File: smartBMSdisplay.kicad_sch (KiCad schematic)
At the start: 7 parts, among them J1 Conn_01x04_Male, J2 Conn_01x05_Male, Q1 BC547, U1 esp32_WROOM

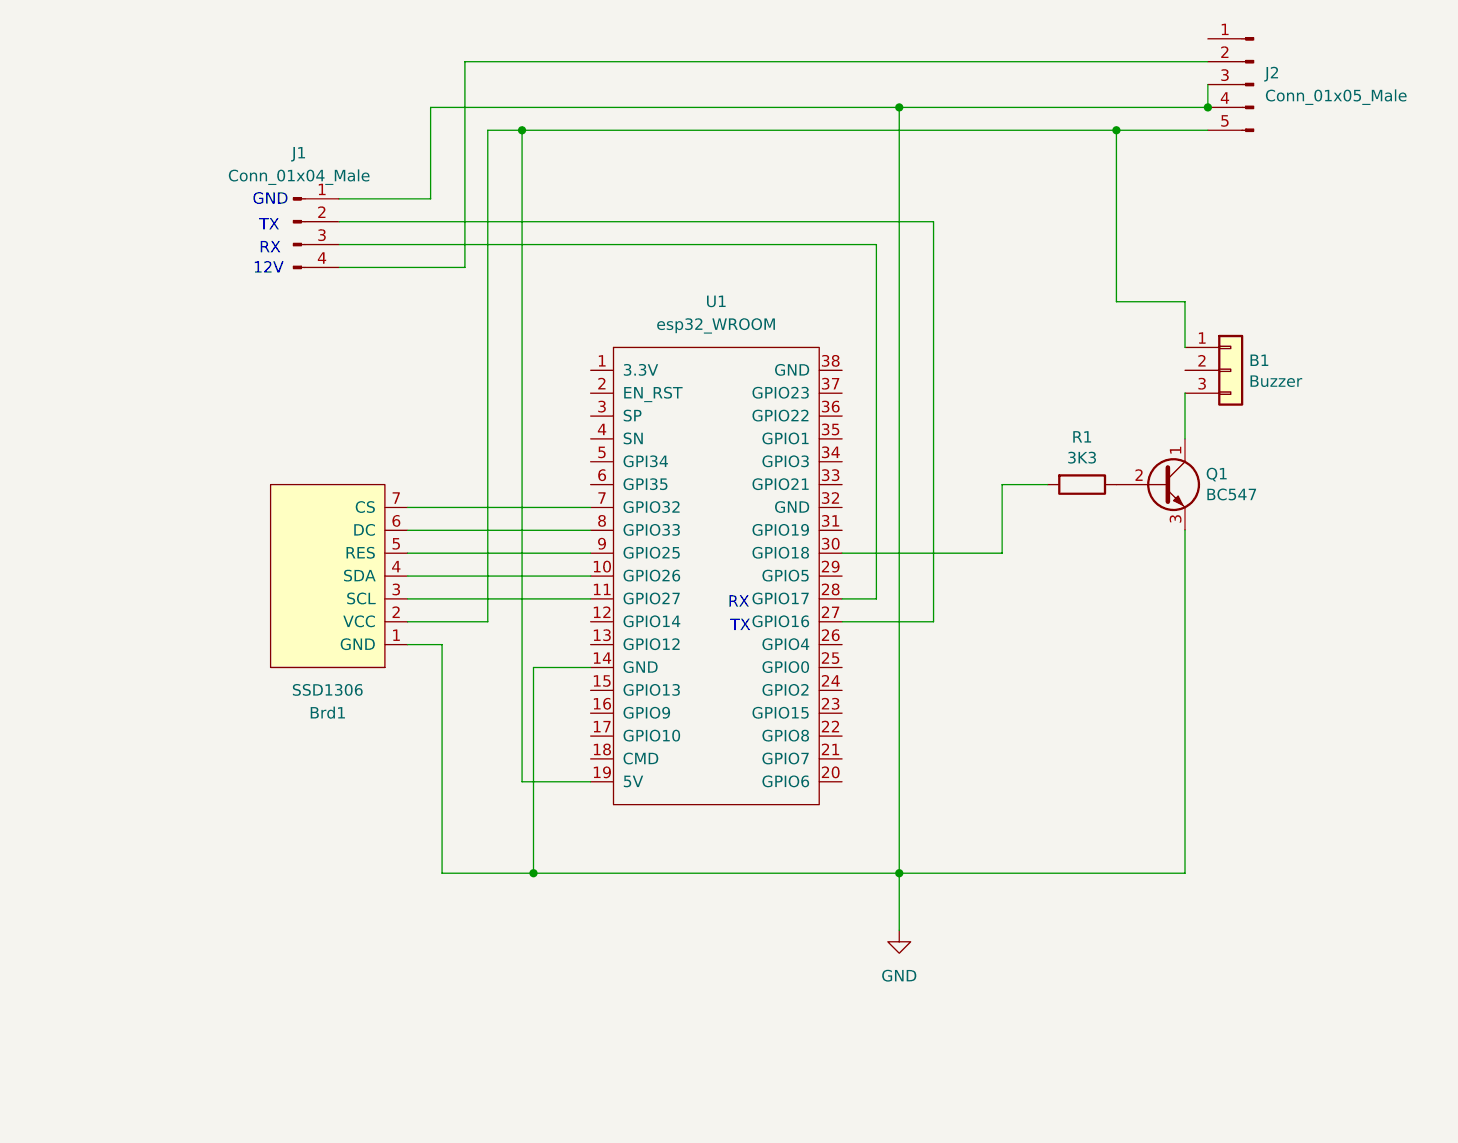
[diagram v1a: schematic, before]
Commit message: Update Readme, misc display changes, update PCB
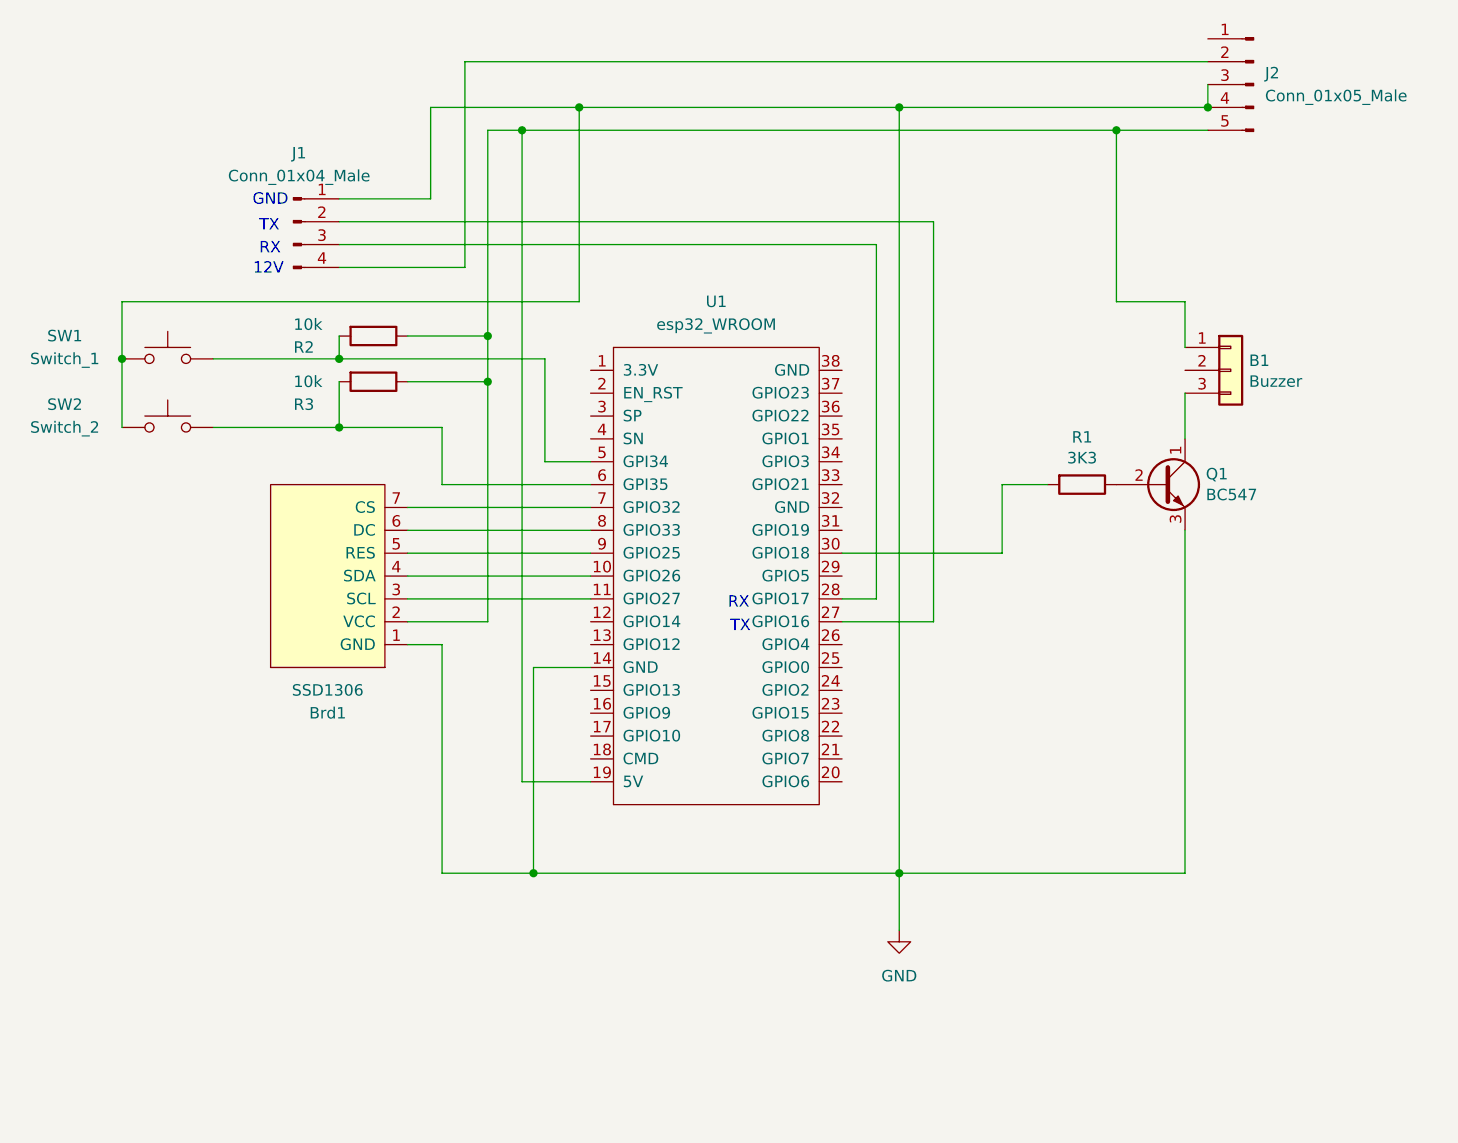
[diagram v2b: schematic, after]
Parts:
- added R2, R3: 10k, Resistor_THT:R_Axial_DIN0207_L6.3mm_D2.5mm_P10.16mm_Horizontal, symbol Device:R
- added SW1: Switch_1, Button_Switch_THT:SW_Tactile_Straight_KSA0Axx1LFTR, symbol Switch:SW_Push
- added SW2: Switch_2, Button_Switch_THT:SW_Tactile_Straight_KSA0Axx1LFTR, symbol Switch:SW_Push
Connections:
- net GND: now also SW1.2, SW2.2
- net at B1.1 (Pin_1), Brd1.2 (VCC), J2.5 (Pin_5)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: now also R2.1, R3.1
- net at U1.5 (GPI34): now also R2.2, SW1.1
- net at U1.6 (GPI35): now also R3.2, SW2.1
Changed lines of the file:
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@@
   (junction (at 144.78 58.42) (diameter 0) (color 0 0 0 0)
   )
+  (junction (at 109.22 58.42) (diameter 0) (color 0 0 0 0)
+  )
   (junction (at 144.78 143.51) (diameter 0) (color 0 0 0 0)
   )
+  (junction (at 82.55 86.36) (diameter 0) (color 0 0 0 0)
+  )
+  (junction (at 58.42 86.36) (diameter 0) (color 0 0 0 0)
+  )
+  (junction (at 82.55 93.98) (diameter 0) (color 0 0 0 0)
+  )
   (junction (at 102.87 60.96) (diameter 0) (color 0 0 0 0)
   )
+  (junction (at 99.06 88.9) (diameter 0) (color 0 0 0 0)
+  )
   (junction (at 168.91 60.96) (diameter 0) (color 0 0 0 0)
   )
+  (junction (at 99.06 83.82) (diameter 0) (color 0 0 0 0)
+  )
+  (wire (pts (xy 109.22 58.42) (xy 144.78 58.42))
+    (stroke (width 0) (type default) (color 0 0 0 0))
+  )
   (wire (pts (xy 176.53 143.51) (xy 144.78 143.51))
     (stroke (width 0) (type default) (color 0 0 0 0))
@@
     (stroke (width 0) (type default) (color 0 0 0 0))
   )
+  (wire (pts (xy 93.98 93.98) (xy 93.98 100.33))
+    (stroke (width 0) (type default) (color 0 0 0 0))
+  )
   (wire (pts (xy 144.78 58.42) (xy 144.78 143.51))
     (stroke (width 0) (type default) (color 0 0 0 0))
   )
+  (wire (pts (xy 68.58 86.36) (xy 82.55 86.36))
+    (stroke (width 0) (type default) (color 0 0 0 0))
+  )
+  (wire (pts (xy 93.98 100.33) (xy 110.49 100.33))
+    (stroke (width 0) (type default) (color 0 0 0 0))
+  )
   (wire (pts (xy 90.17 118.11) (xy 93.98 118.11))
     (stroke (width 0) (type default) (color 0 0 0 0))
@@
     (stroke (width 0) (type default) (color 0 0 0 0))
   )
+  (wire (pts (xy 82.55 83.82) (xy 82.55 86.36))
+    (stroke (width 0) (type default) (color 0 0 0 0))
+  )
   (wire (pts (xy 104.14 120.65) (xy 110.49 120.65))
     (stroke (width 0) (type default) (color 0 0 0 0))
   )
+  (wire (pts (xy 102.87 60.96) (xy 168.91 60.96))
+    (stroke (width 0) (type default) (color 0 0 0 0))
+  )
   (wire (pts (xy 90.17 107.95) (xy 110.49 107.95))
     (stroke (width 0) (type default) (color 0 0 0 0))
   )
-  (wire (pts (xy 102.87 60.96) (xy 168.91 60.96))
-    (stroke (width 0) (type default) (color 0 0 0 0))
-  )
   (wire (pts (xy 168.91 60.96) (xy 168.91 80.01))
     (stroke (width 0) (type default) (color 0 0 0 0))
@@
     (stroke (width 0) (type default) (color 0 0 0 0))
   )
+  (wire (pts (xy 58.42 86.36) (xy 58.42 93.98))
+    (stroke (width 0) (type default) (color 0 0 0 0))
+  )
   (wire (pts (xy 102.87 133.35) (xy 102.87 60.96))
     (stroke (width 0) (type default) (color 0 0 0 0))
   )
+  (wire (pts (xy 90.17 88.9) (xy 99.06 88.9))
+    (stroke (width 0) (type default) (color 0 0 0 0))
+  )
   (wire (pts (xy 90.17 110.49) (xy 110.49 110.49))
     (stroke (width 0) (type default) (color 0 0 0 0))
   )
+  (wire (pts (xy 82.55 93.98) (xy 93.98 93.98))
+    (stroke (width 0) (type default) (color 0 0 0 0))
+  )
   (wire (pts (xy 104.14 143.51) (xy 104.14 120.65))
     (stroke (width 0) (type default) (color 0 0 0 0))
@@
     (stroke (width 0) (type default) (color 0 0 0 0))
   )
+  (wire (pts (xy 96.52 53.34) (xy 179.07 53.34))
+    (stroke (width 0) (type default) (color 0 0 0 0))
+  )
+  (wire (pts (xy 105.41 97.79) (xy 110.49 97.79))
+    (stroke (width 0) (type default) (color 0 0 0 0))
+  )
+  (wire (pts (xy 105.41 86.36) (xy 105.41 97.79))
+    (stroke (width 0) (type default) (color 0 0 0 0))
+  )
   (wire (pts (xy 82.55 71.12) (xy 148.59 71.12))
     (stroke (width 0) (type default) (color 0 0 0 0))
   )
-  (wire (pts (xy 179.07 53.34) (xy 96.52 53.34))
+  (wire (pts (xy 58.42 80.01) (xy 109.22 80.01))
+    (stroke (width 0) (type default) (color 0 0 0 0))
+  )
+  (wire (pts (xy 99.06 83.82) (xy 99.06 60.96))
     (stroke (width 0) (type default) (color 0 0 0 0))
   )
@@
     (stroke (width 0) (type default) (color 0 0 0 0))
   )
+  (wire (pts (xy 68.58 93.98) (xy 82.55 93.98))
+    (stroke (width 0) (type default) (color 0 0 0 0))
+  )
+  (wire (pts (xy 99.06 88.9) (xy 99.06 83.82))
+    (stroke (width 0) (type default) (color 0 0 0 0))
+  )
   (wire (pts (xy 90.17 102.87) (xy 110.49 102.87))
     (stroke (width 0) (type default) (color 0 0 0 0))
   )
+  (wire (pts (xy 82.55 88.9) (xy 82.55 93.98))
+    (stroke (width 0) (type default) (color 0 0 0 0))
+  )
+  (wire (pts (xy 92.71 58.42) (xy 109.22 58.42))
+    (stroke (width 0) (type default) (color 0 0 0 0))
+  )
   (wire (pts (xy 161.29 100.33) (xy 156.21 100.33))
     (stroke (width 0) (type default) (color 0 0 0 0))
@@
     (stroke (width 0) (type default) (color 0 0 0 0))
   )
-  (wire (pts (xy 92.71 58.42) (xy 144.78 58.42))
+  (wire (pts (xy 90.17 83.82) (xy 99.06 83.82))
     (stroke (width 0) (type default) (color 0 0 0 0))
   )
@@
     (stroke (width 0) (type default) (color 0 0 0 0))
   )
+  (wire (pts (xy 82.55 86.36) (xy 105.41 86.36))
+    (stroke (width 0) (type default) (color 0 0 0 0))
+  )
   (wire (pts (xy 156.21 107.95) (xy 138.43 107.95))
     (stroke (width 0) (type default) (color 0 0 0 0))
@@
     (stroke (width 0) (type default) (color 0 0 0 0))
   )
-  (wire (pts (xy 99.06 115.57) (xy 99.06 60.96))
+  (wire (pts (xy 109.22 80.01) (xy 109.22 58.42))
+    (stroke (width 0) (type default) (color 0 0 0 0))
+  )
+  (wire (pts (xy 99.06 115.57) (xy 99.06 88.9))
     (stroke (width 0) (type default) (color 0 0 0 0))
   )
@@
     (stroke (width 0) (type default) (color 0 0 0 0))
   )
+  (wire (pts (xy 58.42 86.36) (xy 58.42 80.01))
+    (stroke (width 0) (type default) (color 0 0 0 0))
+  )
   (wire (pts (xy 176.53 80.01) (xy 168.91 80.01))
     (stroke (width 0) (type default) (color 0 0 0 0))
@@
   (text "RX" (at 73.66 74.93 0)
     (effects (font (size 1.27 1.27)) (justify left bottom))
+  )
+  (symbol (lib_id "Device:R") (at 86.36 88.9 270) (unit 1)
+    (in_bom yes) (on_board yes)
+    (property "Reference" "R3" (id 0) (at 77.47 91.44 90)
+      (effects (font (size 1.27 1.27)) (justify left))
+    )
+    (property "Value" "10k" (id 1) (at 77.47 88.9 90)
+      (effects (font (size 1.27 1.27)) (justify left))
+    )
+    (property "Footprint" "Resistor_THT:R_Axial_DIN0207_L6.3mm_D2.5mm_P10.16mm_Horizontal" (id 2) (at 86.36 87.122 90)
+      (effects (font (size 1.27 1.27)) hide)
+    )
+    (property "Datasheet" "~" (id 3) (at 86.36 88.9 0)
+      (effects (font (size 1.27 1.27)) hide)
+    )
+    (pin "1")
+    (pin "2")
   )
   (symbol (lib_id "Connector:Conn_01x05_Male") (at 184.15 55.88 0) (mirror y) (unit 1)
@@
     )
     (property "Datasheet" "~" (id 3) (at 165.1 100.33 0)
+      (effects (font (size 1.27 1.27)) hide)
+    )
+    (pin "1")
+    (pin "2")
+  )
+  (symbol (lib_id "Device:R") (at 86.36 83.82 270) (unit 1)
+    (in_bom yes) (on_board yes)
+    (property "Reference" "R2" (id 0) (at 77.47 85.09 90)
+      (effects (font (size 1.27 1.27)) (justify left))
+    )
+    (property "Value" "10k" (id 1) (at 77.47 82.55 90)
+      (effects (font (size 1.27 1.27)) (justify left))
+    )
+    (property "Footprint" "Resistor_THT:R_Axial_DIN0207_L6.3mm_D2.5mm_P10.16mm_Horizontal" (id 2) (at 86.36 82.042 90)
+      (effects (font (size 1.27 1.27)) hide)
+    )
+    (property "Datasheet" "~" (id 3) (at 86.36 83.82 0)
+      (effects (font (size 1.27 1.27)) hide)
+    )
+    (pin "1")
+    (pin "2")
+  )
+  (symbol (lib_id "Switch:SW_Push") (at 63.5 86.36 0) (mirror y) (unit 1)
+    (in_bom yes) (on_board yes)
+    (property "Reference" "SW1" (id 0) (at 52.07 83.82 0))
+    (property "Value" "Switch_1" (id 1) (at 52.07 86.36 0))
+    (property "Footprint" "Button_Switch_THT:SW_Tactile_Straight_KSA0Axx1LFTR" (id 2) (at 63.5 81.28 0)
+      (effects (font (size 1.27 1.27)) hide)
+    )
+    (property "Datasheet" "~" (id 3) (at 63.5 81.28 0)
       (effects (font (size 1.27 1.27)) hide)
     )
@@
     (pin "2")
     (pin "3")
+  )
+  (symbol (lib_id "Switch:SW_Push") (at 63.5 93.98 0) (mirror y) (unit 1)
+    (in_bom yes) (on_board yes)
+    (property "Reference" "SW2" (id 0) (at 52.07 91.44 0))
+    (property "Value" "Switch_2" (id 1) (at 52.07 93.98 0))
+    (property "Footprint" "Button_Switch_THT:SW_Tactile_Straight_KSA0Axx1LFTR" (id 2) (at 63.5 88.9 0)
+      (effects (font (size 1.27 1.27)) hide)
+    )
+    (property "Datasheet" "~" (id 3) (at 63.5 88.9 0)
+      (effects (font (size 1.27 1.27)) hide)
+    )
+    (pin "1")
+    (pin "2")
   )
   (symbol (lib_id "SSD1306-128x64_OLED:SSD1306") (at 81.28 114.3 270) (mirror x) (unit 1)
@@
       (reference "R1") (unit 1) (value "3K3") (footprint "Resistor_THT:R_Axial_DIN0207_L6.3mm_D2.5mm_P10.16mm_Horizontal")
     )
+    (path "/6650d055-dffc-4b8f-964b-17e0cea695cf"
+      (reference "R2") (unit 1) (value "10k") (footprint "Resistor_THT:R_Axial_DIN0207_L6.3mm_D2.5mm_P10.16mm_Horizontal")
+    )
+    (path "/08385774-0b14-46cd-9e08-90894ab24973"
+      (reference "R3") (unit 1) (value "10k") (footprint "Resistor_THT:R_Axial_DIN0207_L6.3mm_D2.5mm_P10.16mm_Horizontal")
+    )
+    (path "/77168115-06d5-435e-92cc-4c8abef8cf6c"
+      (reference "SW1") (unit 1) (value "Switch_1") (footprint "Button_Switch_THT:SW_Tactile_Straight_KSA0Axx1LFTR")
+    )
+    (path "/e19c51f0-09c0-441c-a6c5-9c4688d016f8"
+      (reference "SW2") (unit 1) (value "Switch_2") (footprint "Button_Switch_THT:SW_Tactile_Straight_KSA0Axx1LFTR")
+    )
     (path "/fa7cc373-1e9b-4a68-961b-8c9f216ebb9e"
